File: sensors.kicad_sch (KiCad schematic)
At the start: 9 parts, among them IC4 BME690, U2 BME280, U3 BMP581

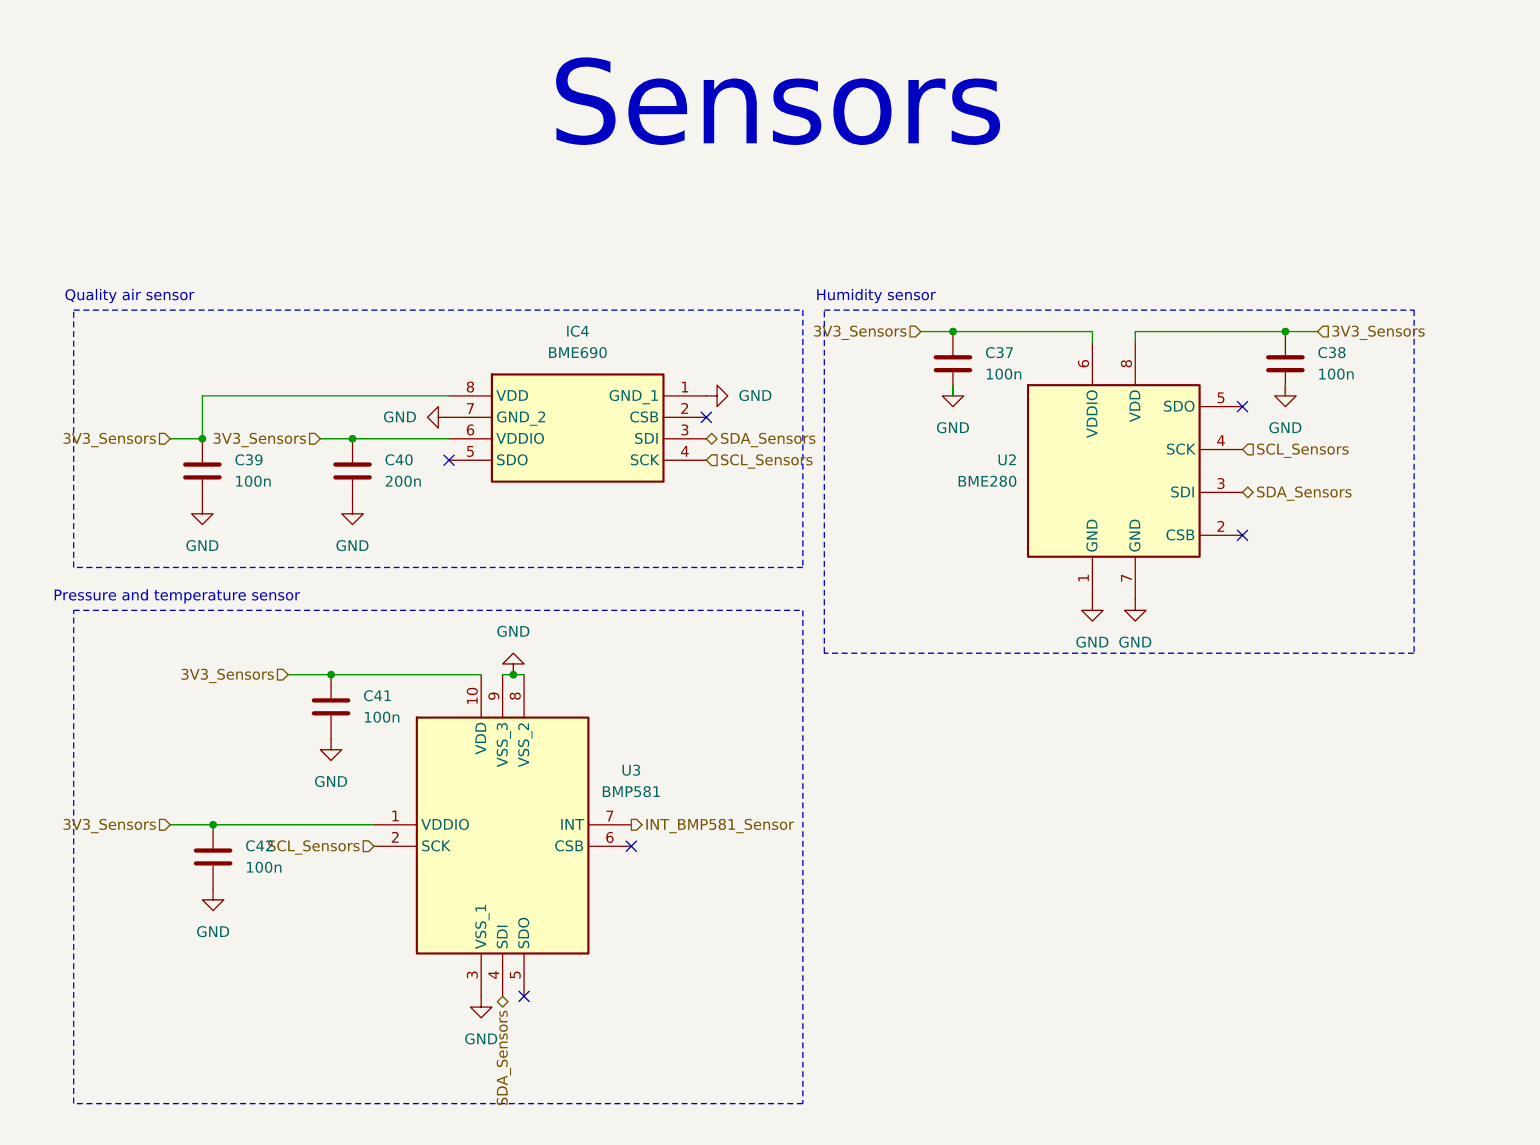
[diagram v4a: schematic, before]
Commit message: Place MCU and its components around
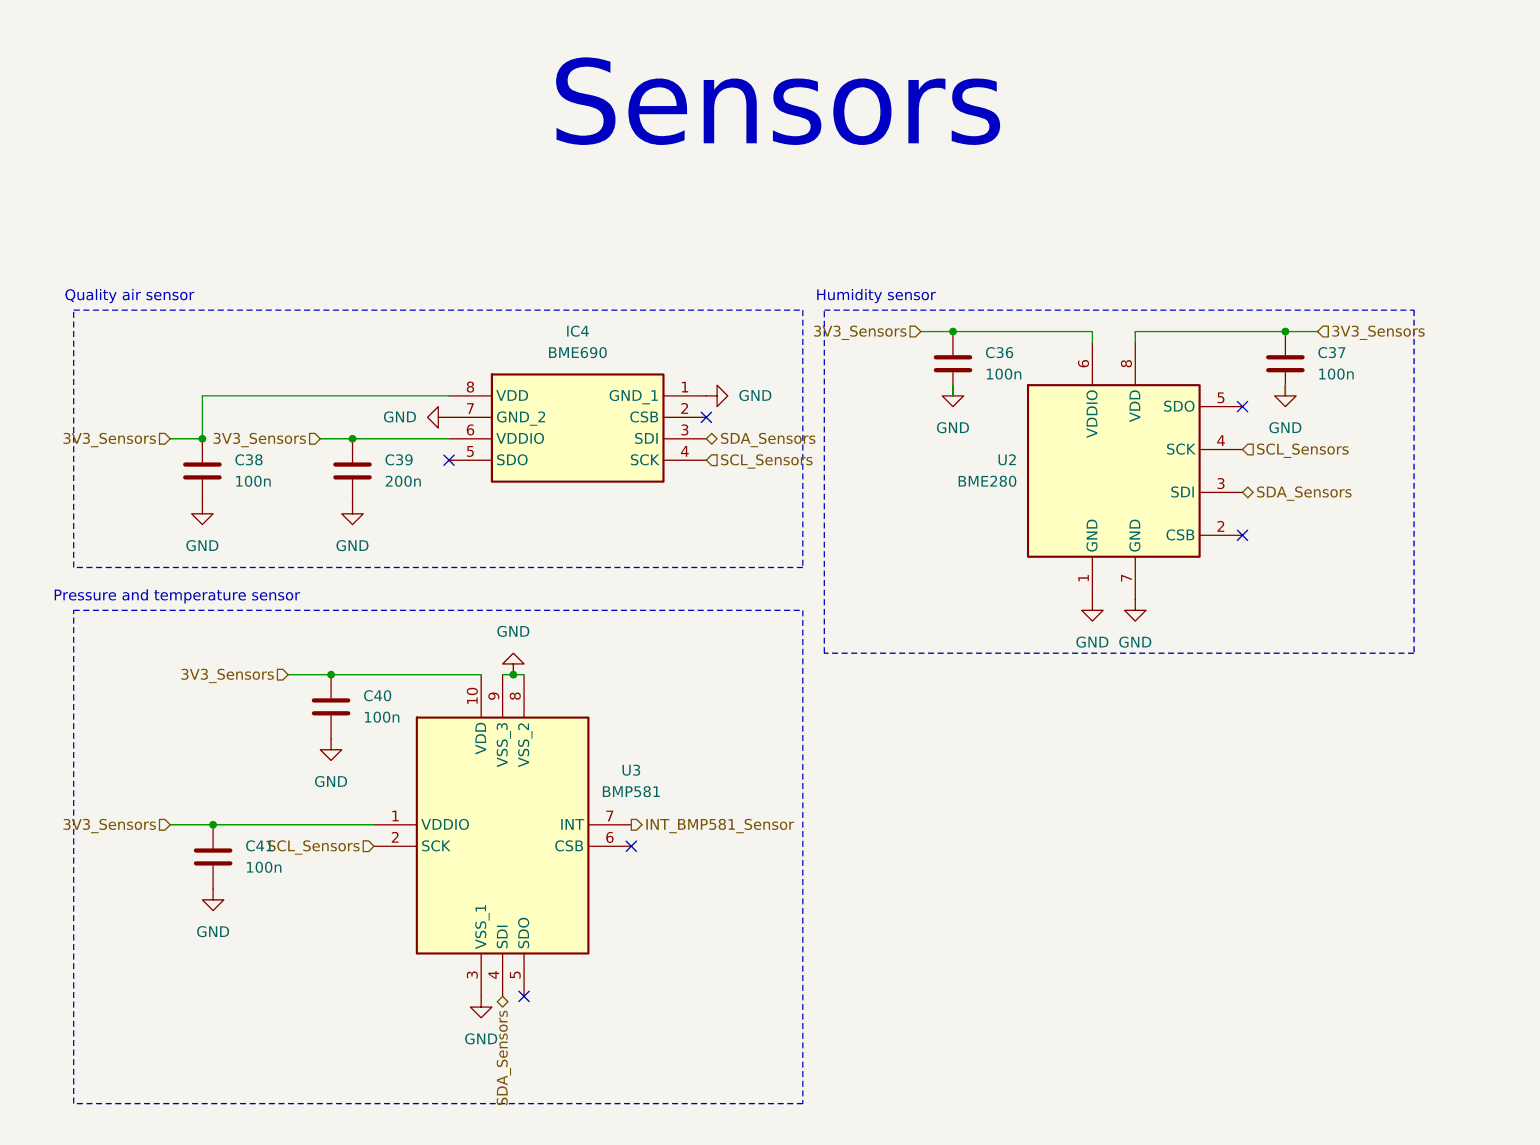
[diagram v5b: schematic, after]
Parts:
- renumbered C37 to C36, C38 to C37, C39 to C38, C40 to C39, C41 to C40, C42 to C41
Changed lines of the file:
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@@
 		(dnp no)
 		(fields_autoplaced yes)
-		(property "Reference" "#PWR059"
+		(property "Reference" "#PWR058"
 			(at 170.18 66.04 0)
 			(effects
@@
 			(project "weather-station-poc"
 				(path "/38eb53bb-294e-46e4-ad59-fd355ca373b9/29574217-d56b-4a63-a2c4-128dfec2758e"
-					(reference "#PWR059")
+					(reference "#PWR058")
 					(unit 1)
 				)
@@
 		(dnp no)
 		(fields_autoplaced yes)
-		(property "Reference" "#PWR061"
+		(property "Reference" "#PWR060"
 			(at 147.32 60.96 0)
 			(effects
@@
 			(project "weather-station-poc"
 				(path "/38eb53bb-294e-46e4-ad59-fd355ca373b9/29574217-d56b-4a63-a2c4-128dfec2758e"
-					(reference "#PWR061")
+					(reference "#PWR060")
 					(unit 1)
 				)
@@
 		(dnp no)
 		(fields_autoplaced yes)
-		(property "Reference" "C38"
+		(property "Reference" "C37"
 			(at 213.36 55.8799 0)
 			(effects
@@
 			(project "weather-station-poc"
 				(path "/38eb53bb-294e-46e4-ad59-fd355ca373b9/29574217-d56b-4a63-a2c4-128dfec2758e"
-					(reference "C38")
+					(reference "C37")
 					(unit 1)
 				)
@@
 		(dnp no)
 		(fields_autoplaced yes)
-		(property "Reference" "C39"
+		(property "Reference" "C38"
 			(at 85.09 68.5799 0)
 			(effects
@@
 			(project ""
 				(path "/38eb53bb-294e-46e4-ad59-fd355ca373b9/29574217-d56b-4a63-a2c4-128dfec2758e"
-					(reference "C39")
+					(reference "C38")
 					(unit 1)
 				)
@@
 		(dnp no)
 		(fields_autoplaced yes)
-		(property "Reference" "#PWR063"
+		(property "Reference" "#PWR062"
 			(at 81.28 80.01 0)
 			(effects
@@
 			(project ""
 				(path "/38eb53bb-294e-46e4-ad59-fd355ca373b9/29574217-d56b-4a63-a2c4-128dfec2758e"
-					(reference "#PWR063")
+					(reference "#PWR062")
 					(unit 1)
 				)
@@
 		(dnp no)
 		(fields_autoplaced yes)
-		(property "Reference" "#PWR066"
+		(property "Reference" "#PWR065"
 			(at 191.77 91.44 0)
 			(effects
@@
 			(project "weather-station-poc"
 				(path "/38eb53bb-294e-46e4-ad59-fd355ca373b9/29574217-d56b-4a63-a2c4-128dfec2758e"
-					(reference "#PWR066")
+					(reference "#PWR065")
 					(unit 1)
 				)
@@
 		(dnp no)
 		(fields_autoplaced yes)
-		(property "Reference" "#PWR067"
+		(property "Reference" "#PWR066"
 			(at 118.11 87.63 0)
 			(effects
@@
 			(project "weather-station-poc"
 				(path "/38eb53bb-294e-46e4-ad59-fd355ca373b9/29574217-d56b-4a63-a2c4-128dfec2758e"
-					(reference "#PWR067")
+					(reference "#PWR066")
 					(unit 1)
 				)
@@
 		(dnp no)
 		(fields_autoplaced yes)
-		(property "Reference" "C40"
+		(property "Reference" "C39"
 			(at 102.87 68.5799 0)
 			(effects
@@
 			(project "weather-station-poc"
 				(path "/38eb53bb-294e-46e4-ad59-fd355ca373b9/29574217-d56b-4a63-a2c4-128dfec2758e"
-					(reference "C40")
+					(reference "C39")
 					(unit 1)
 				)
@@
 		(dnp no)
 		(fields_autoplaced yes)
-		(property "Reference" "#PWR064"
+		(property "Reference" "#PWR063"
 			(at 99.06 80.01 0)
 			(effects
@@
 			(project "weather-station-poc"
 				(path "/38eb53bb-294e-46e4-ad59-fd355ca373b9/29574217-d56b-4a63-a2c4-128dfec2758e"
-					(reference "#PWR064")
+					(reference "#PWR063")
 					(unit 1)
 				)
@@
 		(dnp no)
 		(fields_autoplaced yes)
-		(property "Reference" "#PWR060"
+		(property "Reference" "#PWR059"
 			(at 209.55 66.04 0)
 			(effects
@@
 			(project "weather-station-poc"
 				(path "/38eb53bb-294e-46e4-ad59-fd355ca373b9/29574217-d56b-4a63-a2c4-128dfec2758e"
-					(reference "#PWR060")
+					(reference "#PWR059")
 					(unit 1)
 				)
@@
 		(dnp no)
 		(fields_autoplaced yes)
-		(property "Reference" "#PWR069"
+		(property "Reference" "#PWR068"
 			(at 82.55 125.73 0)
 			(effects
@@
 			(project "weather-station-poc"
 				(path "/38eb53bb-294e-46e4-ad59-fd355ca373b9/29574217-d56b-4a63-a2c4-128dfec2758e"
-					(reference "#PWR069")
+					(reference "#PWR068")
 					(unit 1)
 				)
@@
 		(dnp no)
 		(fields_autoplaced yes)
-		(property "Reference" "#PWR068"
+		(property "Reference" "#PWR067"
 			(at 96.52 107.95 0)
 			(effects
@@
 			(project "weather-station-poc"
 				(path "/38eb53bb-294e-46e4-ad59-fd355ca373b9/29574217-d56b-4a63-a2c4-128dfec2758e"
-					(reference "#PWR068")
+					(reference "#PWR067")
 					(unit 1)
 				)
@@
 		(dnp no)
 		(fields_autoplaced yes)
-		(property "Reference" "#PWR070"
+		(property "Reference" "#PWR069"
 			(at 114.3 138.43 0)
 			(effects
@@
 			(project "weather-station-poc"
 				(path "/38eb53bb-294e-46e4-ad59-fd355ca373b9/29574217-d56b-4a63-a2c4-128dfec2758e"
-					(reference "#PWR070")
+					(reference "#PWR069")
 					(unit 1)
 				)
@@
 		(dnp no)
 		(fields_autoplaced yes)
-		(property "Reference" "#PWR062"
+		(property "Reference" "#PWR061"
 			(at 104.14 63.5 0)
 			(effects
@@
 			(project "weather-station-poc"
 				(path "/38eb53bb-294e-46e4-ad59-fd355ca373b9/29574217-d56b-4a63-a2c4-128dfec2758e"
-					(reference "#PWR062")
+					(reference "#PWR061")
 					(unit 1)
 				)
@@
 		(dnp no)
 		(fields_autoplaced yes)
-		(property "Reference" "C42"
+		(property "Reference" "C41"
 			(at 86.36 114.2999 0)
 			(effects
@@
 			(project "weather-station-poc"
 				(path "/38eb53bb-294e-46e4-ad59-fd355ca373b9/29574217-d56b-4a63-a2c4-128dfec2758e"
-					(reference "C42")
+					(reference "C41")
 					(unit 1)
 				)
@@
 		(dnp no)
 		(fields_autoplaced yes)
-		(property "Reference" "#PWR065"
+		(property "Reference" "#PWR064"
 			(at 186.69 91.44 0)
 			(effects
@@
 			(project "weather-station-poc"
 				(path "/38eb53bb-294e-46e4-ad59-fd355ca373b9/29574217-d56b-4a63-a2c4-128dfec2758e"
-					(reference "#PWR065")
+					(reference "#PWR064")
 					(unit 1)
 				)
@@
 		(dnp no)
 		(fields_autoplaced yes)
-		(property "Reference" "C41"
+		(property "Reference" "C40"
 			(at 100.33 96.5199 0)
 			(effects
@@
 			(project "weather-station-poc"
 				(path "/38eb53bb-294e-46e4-ad59-fd355ca373b9/29574217-d56b-4a63-a2c4-128dfec2758e"
-					(reference "C41")
+					(reference "C40")
 					(unit 1)
 				)
@@
 		(dnp no)
 		(fields_autoplaced yes)
-		(property "Reference" "C37"
+		(property "Reference" "C36"
 			(at 173.99 55.8799 0)
 			(effects
@@
 			(project "weather-station-poc"
 				(path "/38eb53bb-294e-46e4-ad59-fd355ca373b9/29574217-d56b-4a63-a2c4-128dfec2758e"
-					(reference "C37")
-					(unit 1)
-				)
+					(reference "C36")
+					(unit 1)
+				)

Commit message: Place all components on the PCB correctly
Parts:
- renumbered C36 to C37, C37 to C38, C38 to C39, C39 to C40, C40 to C41, C41 to C42
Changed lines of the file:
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@@
 		(dnp no)
 		(fields_autoplaced yes)
-		(property "Reference" "#PWR058"
+		(property "Reference" "#PWR059"
 			(at 170.18 66.04 0)
 			(effects
@@
 			(project "weather-station-poc"
 				(path "/38eb53bb-294e-46e4-ad59-fd355ca373b9/29574217-d56b-4a63-a2c4-128dfec2758e"
-					(reference "#PWR058")
+					(reference "#PWR059")
 					(unit 1)
 				)
@@
 		(dnp no)
 		(fields_autoplaced yes)
-		(property "Reference" "#PWR060"
+		(property "Reference" "#PWR061"
 			(at 147.32 60.96 0)
 			(effects
@@
 			(project "weather-station-poc"
 				(path "/38eb53bb-294e-46e4-ad59-fd355ca373b9/29574217-d56b-4a63-a2c4-128dfec2758e"
-					(reference "#PWR060")
+					(reference "#PWR061")
 					(unit 1)
 				)
@@
 		(dnp no)
 		(fields_autoplaced yes)
-		(property "Reference" "C37"
+		(property "Reference" "C38"
 			(at 213.36 55.8799 0)
 			(effects
@@
 			(project "weather-station-poc"
 				(path "/38eb53bb-294e-46e4-ad59-fd355ca373b9/29574217-d56b-4a63-a2c4-128dfec2758e"
-					(reference "C37")
+					(reference "C38")
 					(unit 1)
 				)
@@
 		(dnp no)
 		(fields_autoplaced yes)
-		(property "Reference" "C38"
+		(property "Reference" "C39"
 			(at 85.09 68.5799 0)
 			(effects
@@
 			(project ""
 				(path "/38eb53bb-294e-46e4-ad59-fd355ca373b9/29574217-d56b-4a63-a2c4-128dfec2758e"
-					(reference "C38")
+					(reference "C39")
 					(unit 1)
 				)
@@
 		(dnp no)
 		(fields_autoplaced yes)
-		(property "Reference" "#PWR062"
+		(property "Reference" "#PWR063"
 			(at 81.28 80.01 0)
 			(effects
@@
 			(project ""
 				(path "/38eb53bb-294e-46e4-ad59-fd355ca373b9/29574217-d56b-4a63-a2c4-128dfec2758e"
-					(reference "#PWR062")
+					(reference "#PWR063")
 					(unit 1)
 				)
@@
 		(dnp no)
 		(fields_autoplaced yes)
-		(property "Reference" "#PWR065"
+		(property "Reference" "#PWR066"
 			(at 191.77 91.44 0)
 			(effects
@@
 			(project "weather-station-poc"
 				(path "/38eb53bb-294e-46e4-ad59-fd355ca373b9/29574217-d56b-4a63-a2c4-128dfec2758e"
-					(reference "#PWR065")
+					(reference "#PWR066")
 					(unit 1)
 				)
@@
 		(dnp no)
 		(fields_autoplaced yes)
-		(property "Reference" "#PWR066"
+		(property "Reference" "#PWR067"
 			(at 118.11 87.63 0)
 			(effects
@@
 			(project "weather-station-poc"
 				(path "/38eb53bb-294e-46e4-ad59-fd355ca373b9/29574217-d56b-4a63-a2c4-128dfec2758e"
-					(reference "#PWR066")
+					(reference "#PWR067")
 					(unit 1)
 				)
@@
 		(dnp no)
 		(fields_autoplaced yes)
-		(property "Reference" "C39"
+		(property "Reference" "C40"
 			(at 102.87 68.5799 0)
 			(effects
@@
 			(project "weather-station-poc"
 				(path "/38eb53bb-294e-46e4-ad59-fd355ca373b9/29574217-d56b-4a63-a2c4-128dfec2758e"
-					(reference "C39")
+					(reference "C40")
 					(unit 1)
 				)
@@
 		(dnp no)
 		(fields_autoplaced yes)
-		(property "Reference" "#PWR063"
+		(property "Reference" "#PWR064"
 			(at 99.06 80.01 0)
 			(effects
@@
 			(project "weather-station-poc"
 				(path "/38eb53bb-294e-46e4-ad59-fd355ca373b9/29574217-d56b-4a63-a2c4-128dfec2758e"
-					(reference "#PWR063")
+					(reference "#PWR064")
 					(unit 1)
 				)
@@
 		(dnp no)
 		(fields_autoplaced yes)
-		(property "Reference" "#PWR059"
+		(property "Reference" "#PWR060"
 			(at 209.55 66.04 0)
 			(effects
@@
 			(project "weather-station-poc"
 				(path "/38eb53bb-294e-46e4-ad59-fd355ca373b9/29574217-d56b-4a63-a2c4-128dfec2758e"
-					(reference "#PWR059")
+					(reference "#PWR060")
 					(unit 1)
 				)
@@
 		(dnp no)
 		(fields_autoplaced yes)
-		(property "Reference" "#PWR068"
+		(property "Reference" "#PWR069"
 			(at 82.55 125.73 0)
 			(effects
@@
 			(project "weather-station-poc"
 				(path "/38eb53bb-294e-46e4-ad59-fd355ca373b9/29574217-d56b-4a63-a2c4-128dfec2758e"
-					(reference "#PWR068")
+					(reference "#PWR069")
 					(unit 1)
 				)
@@
 		(dnp no)
 		(fields_autoplaced yes)
-		(property "Reference" "#PWR067"
+		(property "Reference" "#PWR068"
 			(at 96.52 107.95 0)
 			(effects
@@
 			(project "weather-station-poc"
 				(path "/38eb53bb-294e-46e4-ad59-fd355ca373b9/29574217-d56b-4a63-a2c4-128dfec2758e"
-					(reference "#PWR067")
+					(reference "#PWR068")
 					(unit 1)
 				)
@@
 		(dnp no)
 		(fields_autoplaced yes)
-		(property "Reference" "#PWR069"
+		(property "Reference" "#PWR070"
 			(at 114.3 138.43 0)
 			(effects
@@
 			(project "weather-station-poc"
 				(path "/38eb53bb-294e-46e4-ad59-fd355ca373b9/29574217-d56b-4a63-a2c4-128dfec2758e"
-					(reference "#PWR069")
+					(reference "#PWR070")
 					(unit 1)
 				)
@@
 		(dnp no)
 		(fields_autoplaced yes)
-		(property "Reference" "#PWR061"
+		(property "Reference" "#PWR062"
 			(at 104.14 63.5 0)
 			(effects
@@
 			(project "weather-station-poc"
 				(path "/38eb53bb-294e-46e4-ad59-fd355ca373b9/29574217-d56b-4a63-a2c4-128dfec2758e"
-					(reference "#PWR061")
+					(reference "#PWR062")
 					(unit 1)
 				)
@@
 		(dnp no)
 		(fields_autoplaced yes)
-		(property "Reference" "C41"
+		(property "Reference" "C42"
 			(at 86.36 114.2999 0)
 			(effects
@@
 			(project "weather-station-poc"
 				(path "/38eb53bb-294e-46e4-ad59-fd355ca373b9/29574217-d56b-4a63-a2c4-128dfec2758e"
-					(reference "C41")
+					(reference "C42")
 					(unit 1)
 				)
@@
 		(dnp no)
 		(fields_autoplaced yes)
-		(property "Reference" "#PWR064"
+		(property "Reference" "#PWR065"
 			(at 186.69 91.44 0)
 			(effects
@@
 			(project "weather-station-poc"
 				(path "/38eb53bb-294e-46e4-ad59-fd355ca373b9/29574217-d56b-4a63-a2c4-128dfec2758e"
-					(reference "#PWR064")
+					(reference "#PWR065")
 					(unit 1)
 				)
@@
 		(dnp no)
 		(fields_autoplaced yes)
-		(property "Reference" "C40"
+		(property "Reference" "C41"
 			(at 100.33 96.5199 0)
 			(effects
@@
 			(project "weather-station-poc"
 				(path "/38eb53bb-294e-46e4-ad59-fd355ca373b9/29574217-d56b-4a63-a2c4-128dfec2758e"
-					(reference "C40")
+					(reference "C41")
 					(unit 1)
 				)
@@
 		(dnp no)
 		(fields_autoplaced yes)
-		(property "Reference" "C36"
+		(property "Reference" "C37"
 			(at 173.99 55.8799 0)
 			(effects
@@
 			(project "weather-station-poc"
 				(path "/38eb53bb-294e-46e4-ad59-fd355ca373b9/29574217-d56b-4a63-a2c4-128dfec2758e"
-					(reference "C36")
-					(unit 1)
-				)
+					(reference "C37")
+					(unit 1)
+				)
